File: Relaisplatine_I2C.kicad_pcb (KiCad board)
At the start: 2 copper layers, 85.1 x 107.3 mm, 31 parts, among them J1 J, J1.1 G1-J, J1.2 G1-K, J1001 Conn_01x08, J2 K, J2.1 G2-J, J2.2 G2-K, J3.1 G3-J, J3.2 G3-K, J4.1 G4-J, J4.2 G4-K, J5.1 G5-J, J5.2 G5-K, J6.1 G6-J, J6.2 G6-K, J7.1 G7-J, J7.2 G7-K, J8.1 G8-J, J8.2 G8-K, U1 ULN2803A, U2 PCF8574

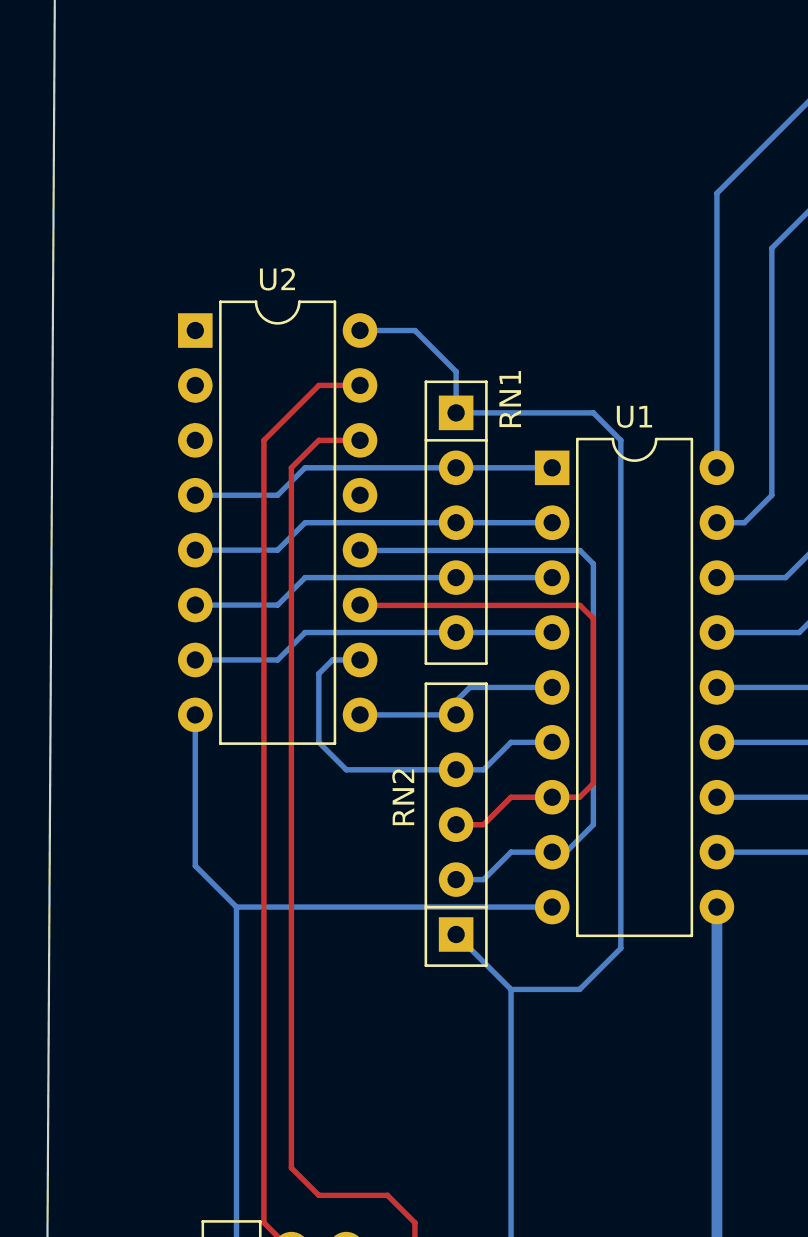
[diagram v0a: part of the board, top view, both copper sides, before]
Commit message: Pins für A0-2 beschltet
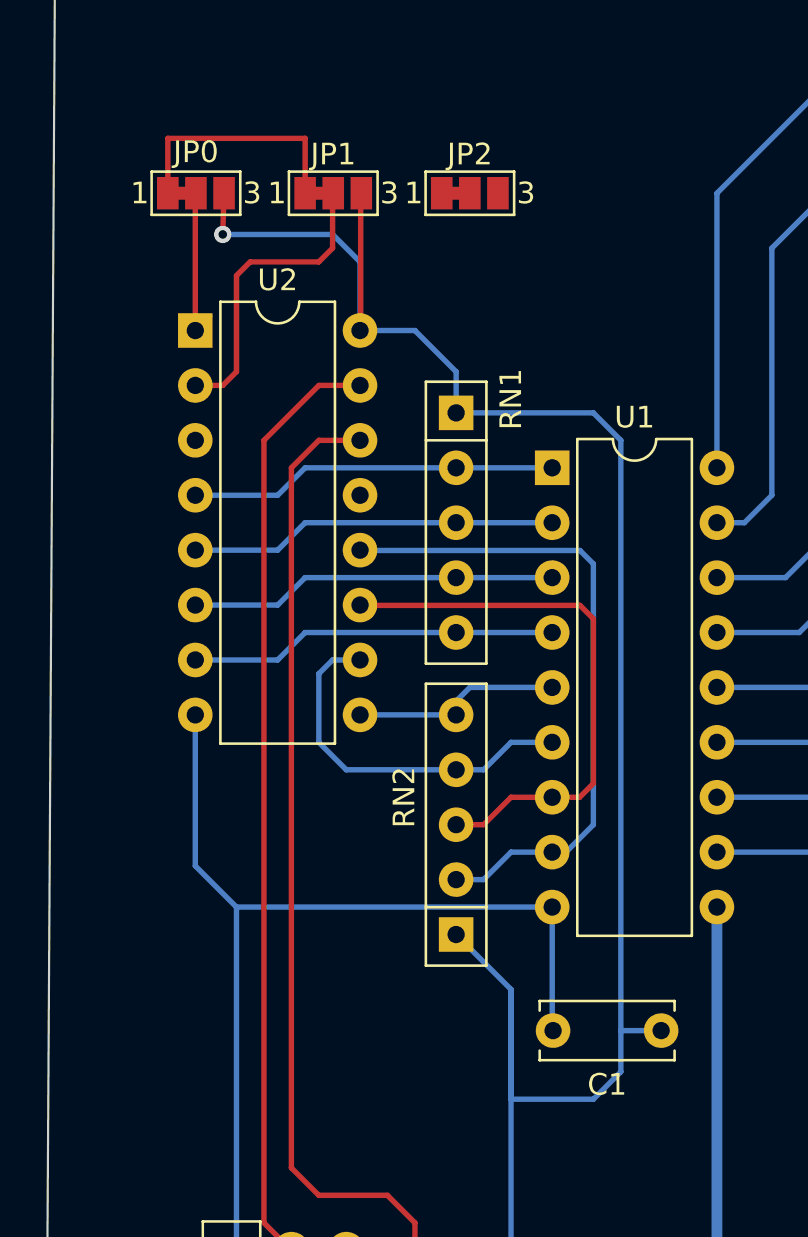
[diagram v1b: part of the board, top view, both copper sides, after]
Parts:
- added C1: 100n, Capacitor_THT:C_Disc_D6.0mm_W2.5mm_P5.00mm, F.Cu at (87.6, 120.0)
- added JP0: SolderJumper_3_Open, Jumper:SolderJumper-3_P1.3mm_Bridged12_Pad1.0x1.5mm_NumberLabels, F.Cu at (66.1, 81.3)
- added JP1: SolderJumper_3_Open, Jumper:SolderJumper-3_P1.3mm_Bridged12_Pad1.0x1.5mm_NumberLabels, F.Cu at (72.4, 81.3)
- added JP2: SolderJumper_3_Open, Jumper:SolderJumper-3_P1.3mm_Bridged12_Pad1.0x1.5mm_NumberLabels, F.Cu at (78.7, 81.3)
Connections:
- U2 pad 1: unconnected-(U2-A0-Pad1) -> Net-(JP0-C)
- U2 pad 2: unconnected-(U2-A1-Pad2) -> Net-(JP1-C)
- U2 pad 3: unconnected-(U2-A2-Pad3) -> Net-(JP2-C)
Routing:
- net +5V: track 72.6 -> 103.4 mm, vias 0 -> 1
- net GND: track 52.5 -> 69.7 mm
- net Net-(JP1-C): track 0.00 -> 14.1 mm
- net Net-(JP0-C): track 0.00 -> 6.63 mm

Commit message: Unbekannte Änderungen
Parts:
- added D1: LED, LED_SMD:LED_0805_2012Metric_Pad1.15x1.40mm_HandSolder, F.Cu at (100.3, 56.9)
- added D2: LED, LED_SMD:LED_0805_2012Metric_Pad1.15x1.40mm_HandSolder, F.Cu at (100.3, 69.6)
- added D3: LED, LED_SMD:LED_0805_2012Metric_Pad1.15x1.40mm_HandSolder, F.Cu at (100.3, 82.3)
- added D4: LED, LED_SMD:LED_0805_2012Metric_Pad1.15x1.40mm_HandSolder, F.Cu at (100.3, 95.0)
- added D5: LED, LED_SMD:LED_0805_2012Metric_Pad1.15x1.40mm_HandSolder, F.Cu at (100.3, 107.7)
- added D6: LED, LED_SMD:LED_0805_2012Metric_Pad1.15x1.40mm_HandSolder, F.Cu at (100.3, 120.4)
- added D7: LED, LED_SMD:LED_0805_2012Metric_Pad1.15x1.40mm_HandSolder, F.Cu at (100.3, 133.1)
- added D8: LED, LED_SMD:LED_0805_2012Metric_Pad1.15x1.40mm_HandSolder, F.Cu at (100.3, 145.8)
- added H1: MountingHole, MountingHole:MountingHole_3.2mm_M3, F.Cu at (67.3, 48.3)
- added H2: MountingHole, MountingHole:MountingHole_3.2mm_M3, F.Cu at (67.3, 154.3)
- added H3: MountingHole, MountingHole:MountingHole_3.2mm_M3, F.Cu at (135.3, 48.3)
- added H4: MountingHole, MountingHole:MountingHole_3.2mm_M3, F.Cu at (135.3, 154.3)
- added J1.1a1001: G1-J, Connector_Pin:Pin_D1.1mm_L8.5mm_W2.5mm_FlatFork, F.Cu at (130.6, 52.7)
- added J1.1a1002: G1-K, Connector_Pin:Pin_D1.1mm_L8.5mm_W2.5mm_FlatFork, F.Cu at (130.6, 86.4)
- added J1.1a1003: G1-K, Connector_Pin:Pin_D1.1mm_L8.5mm_W2.5mm_FlatFork, F.Cu at (130.6, 99.1)
- added J1.1a1004: G1-K, Connector_Pin:Pin_D1.1mm_L8.5mm_W2.5mm_FlatFork, F.Cu at (130.6, 111.8)
- added J1.1a1005: G1-K, Connector_Pin:Pin_D1.1mm_L8.5mm_W2.5mm_FlatFork, F.Cu at (130.6, 124.5)
- added J1.1a1006: G1-K, Connector_Pin:Pin_D1.1mm_L8.5mm_W2.5mm_FlatFork, F.Cu at (130.6, 137.2)
- added J1.1a1007: G1-K, Connector_Pin:Pin_D1.1mm_L8.5mm_W2.5mm_FlatFork, F.Cu at (130.3, 149.9)
- added J1.2a1001: G1-K, Connector_Pin:Pin_D1.1mm_L8.5mm_W2.5mm_FlatFork, F.Cu at (130.6, 61.0)
- added J1.2a1002: G1-J, Connector_Pin:Pin_D1.1mm_L8.5mm_W2.5mm_FlatFork, F.Cu at (130.6, 78.7)
- added J1.2a1003: G1-J, Connector_Pin:Pin_D1.1mm_L8.5mm_W2.5mm_FlatFork, F.Cu at (130.6, 91.4)
- added J1.2a1004: G1-J, Connector_Pin:Pin_D1.1mm_L8.5mm_W2.5mm_FlatFork, F.Cu at (130.6, 104.1)
- added J1.2a1005: G1-J, Connector_Pin:Pin_D1.1mm_L8.5mm_W2.5mm_FlatFork, F.Cu at (130.6, 116.8)
- added J1.2a1006: G1-J, Connector_Pin:Pin_D1.1mm_L8.5mm_W2.5mm_FlatFork, F.Cu at (130.6, 129.5)
- added J1.2a1007: G1-J, Connector_Pin:Pin_D1.1mm_L8.5mm_W2.5mm_FlatFork, F.Cu at (130.6, 142.2)
- added J1001: I²C, Connector_PinHeader_2.54mm:PinHeader_2x02_P2.54mm_Horizontal, F.Cu at (73.0, 147.3)
- added J2.1a1001: G1-J, Connector_Pin:Pin_D1.1mm_L8.5mm_W2.5mm_FlatFork, F.Cu at (130.6, 66.0)
- added J2.2a1001: G2-K, Connector_Pin:Pin_D1.1mm_L8.5mm_W2.5mm_FlatFork, F.Cu at (130.6, 73.7)
- added R1: 1k, Resistor_SMD:R_0805_2012Metric_Pad1.20x1.40mm_HandSolder, F.Cu at (101.3, 61.0)
- added R2: 1k, Resistor_SMD:R_0805_2012Metric_Pad1.20x1.40mm_HandSolder, F.Cu at (101.3, 73.7)
- added R3: 1k, Resistor_SMD:R_0805_2012Metric_Pad1.20x1.40mm_HandSolder, F.Cu at (101.3, 86.4)
- added R4: 1k, Resistor_SMD:R_0805_2012Metric_Pad1.20x1.40mm_HandSolder, F.Cu at (101.4, 99.1)
- added R5: 1k, Resistor_SMD:R_0805_2012Metric_Pad1.20x1.40mm_HandSolder, F.Cu at (101.3, 111.8)
- added R6: 1k, Resistor_SMD:R_0805_2012Metric_Pad1.20x1.40mm_HandSolder, F.Cu at (101.3, 124.5)
- added R7: 1k, Resistor_SMD:R_0805_2012Metric_Pad1.20x1.40mm_HandSolder, F.Cu at (101.3, 137.2)
- added R8: 1k, Resistor_SMD:R_0805_2012Metric_Pad1.20x1.40mm_HandSolder, F.Cu at (101.3, 149.9)
- J1: value J -> K
- J1.1: value G1-J -> G1-K
- J1.2: value G1-K -> G1-J
- J10: renamed from J1001; value Conn_01x08 -> I²C
- J2: value K -> J
- J2.1: value G2-J -> G2-K
- J2.2: value G2-K -> G2-J
- J3.1: value G3-J -> G3-K
- J3.2: value G3-K -> G3-J
- J4.1: value G4-J -> G4-K
- J4.2: value G4-K -> G4-J
- J5.1: value G5-J -> G5-K
- J5.2: value G5-K -> G5-J
- J6.1: value G6-J -> G6-K
- J6.2: value G6-K -> G6-J
- J7.1: value G7-J -> G7-K
- J7.2: value G7-K -> G7-J
- J8.1: value G8-J -> G8-K
- J8.2: value G8-K -> G8-J
- moved C1 50.8 mm to (76.2, 70.5), turned to 0 degrees
- moved A1 41.6 mm to (67.3, 122.6)
- moved A2 37.9 mm to (69.8, 118.1)
- moved A0 36.9 mm to (64.7, 118.1)
- moved U2 25.4 mm to (65.4, 113.0), turned to 90 degrees
- moved RN1 22.2 mm to (69.2, 71.1)
- moved RN2 22.2 mm to (69.2, 95.2)
- moved U1 19.1 mm to (83.8, 74.9)
- moved J1 13.3 mm to (67.3, 63.5)
- moved J2 12.8 mm to (67.3, 55.9)
- moved J8.1 5.21 mm to (138.4, 149.1)
- moved J5.1 5.14 mm to (138.4, 111.3)
- moved J7.1 5.12 mm to (138.4, 136.5)
- moved J6.2 5.12 mm to (138.4, 118.1)
- moved J7.2 5.12 mm to (138.4, 130.8)
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- renumbered JP0 to A0, JP1 to A1, JP2 to A2
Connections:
- RL1 pad 5: unconnected-(RL1-Pad5) -> Net-(J1.2a1001-Pin_1)
- RL1 pad 8: unconnected-(RL1-Pad8) -> Net-(J1.1a1001-Pin_1)
- RL2 pad 5: unconnected-(RL2-Pad5) -> Net-(J2.2a1001-Pin_1)
- RL2 pad 8: unconnected-(RL2-Pad8) -> Net-(J2.1a1001-Pin_1)
- RL3 pad 5: unconnected-(RL3-Pad5) -> Net-(J1.1a1002-Pin_1)
- RL3 pad 8: unconnected-(RL3-Pad8) -> Net-(J1.2a1002-Pin_1)
- RL4 pad 5: unconnected-(RL4-Pad5) -> Net-(J1.1a1003-Pin_1)
- RL4 pad 8: unconnected-(RL4-Pad8) -> Net-(J1.2a1003-Pin_1)
- RL5 pad 5: unconnected-(RL5-Pad5) -> Net-(J1.1a1004-Pin_1)
- RL5 pad 8: unconnected-(RL5-Pad8) -> Net-(J1.2a1004-Pin_1)
- RL6 pad 5: unconnected-(RL6-Pad5) -> Net-(J1.1a1005-Pin_1)
- RL6 pad 8: unconnected-(RL6-Pad8) -> Net-(J1.2a1005-Pin_1)
- RL7 pad 5: unconnected-(RL7-Pad5) -> Net-(J1.1a1006-Pin_1)
- RL7 pad 8: unconnected-(RL7-Pad8) -> Net-(J1.2a1006-Pin_1)
- RL8 pad 5: unconnected-(RL8-Pad5) -> Net-(J1.1a1007-Pin_1)
- RL8 pad 8: unconnected-(RL8-Pad8) -> Net-(J1.2a1007-Pin_1)
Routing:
- net +12V: track 152.1 -> 229.7 mm
- net GND: track 69.7 -> 129.0 mm, vias 0 -> 3
- net Net-(RN1-R1): track 17.0 -> 73.9 mm
- net Net-(RN1-R3): track 17.0 -> 70.5 mm
- net Net-(RN1-R2): track 17.0 -> 62.3 mm
- net Net-(RN1-R4): track 17.0 -> 59.6 mm
- net Net-(RN2-R4): track 9.42 -> 45.5 mm
- net Net-(RN2-R3): track 17.2 -> 40.8 mm
- net +5V: track 103.4 -> 126.9 mm, vias 1 -> 2
- net Net-(D8-K): track 47.6 -> 69.7 mm
- net Net-(D7-K): track 38.3 -> 60.1 mm
- net Net-(D6-K): track 27.2 -> 49.0 mm
- net Net-(D5-K): track 19.8 -> 40.7 mm
- net Net-(J1.1a1004-Pin_1): track 0.00 -> 16.9 mm
- net Net-(J1.1a1002-Pin_1): track 0.00 -> 16.3 mm
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- added copper zone on F.Cu, net +5V
- added copper zone on B.Cu, net GND
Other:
- board size 85.1 x 107.3 mm -> 85.1 x 114.9 mm
- board text added: "+5/12V"
- board text added: "+5V"
- board text added: "G1"
- board text added: "G2"
- board text added: "G3"
- board text added: "G4"
- board text added: "G5"
- board text added: "G6"
- board text added: "G7"
- board text added: "G8"
- board text added: "GND"
- board text added: "Relais"
- board text added: "Relais stromlos"
- board text added: "SCL"
- board text added: "SDA"
- board text added: "©H3-H5N6 2023 I²C Relaisplatine v1.0"

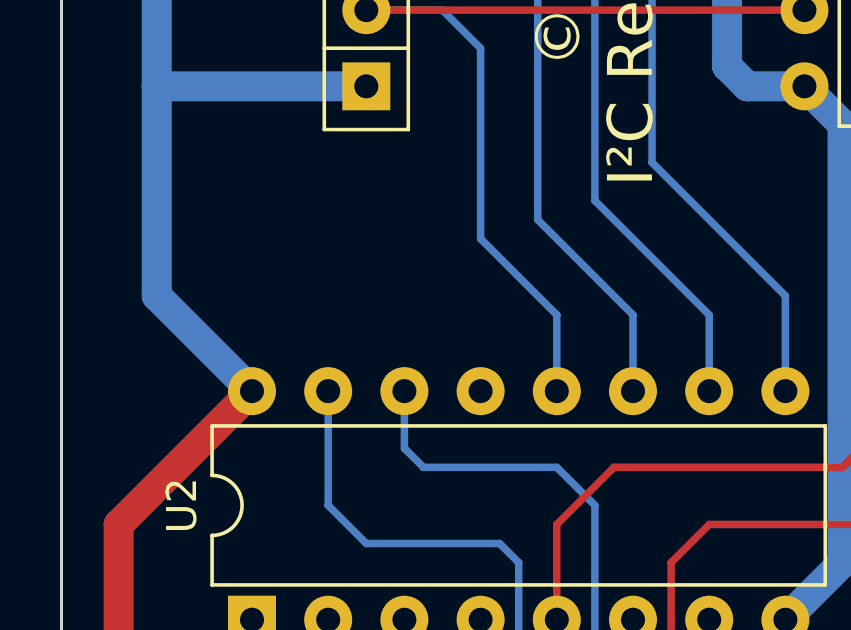
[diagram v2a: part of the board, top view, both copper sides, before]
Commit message: Int-Pin herausgezogen und Kosmetik
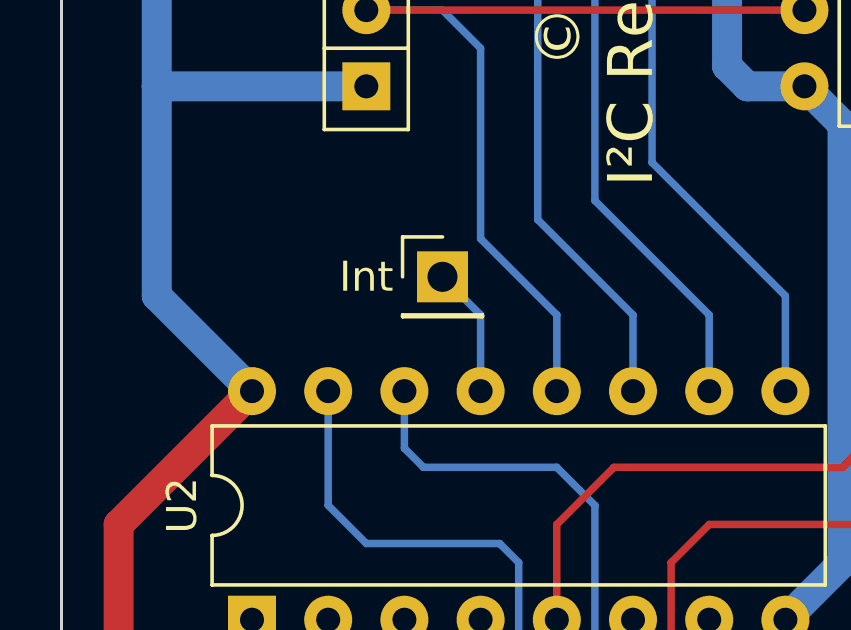
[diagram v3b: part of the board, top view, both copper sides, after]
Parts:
- added J12: Int, Connector_PinHeader_2.54mm:PinHeader_1x01_P2.54mm_Vertical, F.Cu at (71.8, 101.6)
- added Tx1: ©H3-H5N6 2023 I²C Relaisplatine v1.0, Text:Text, F.Cu at (103.8, 46.0)
- J11: renamed from J1001; value I²C -> Relais-Power
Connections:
- U2 pad 13: unconnected-(U2-~{INT}-Pad13) -> Net-(J12-Pin_1)
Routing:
- net Net-(J12-Pin_1): track 0.00 -> 4.34 mm
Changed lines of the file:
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@@
   (net 16 "Net-(A2-C)")
   (net 17 "Net-(A1-C)")
-  (net 18 "unconnected-(U2-~{INT}-Pad13)")
+  (net 18 "Net-(J12-Pin_1)")
   (net 19 "Net-(J1-Pin_1)")
   (net 20 "Net-(J5.2-Pin_1)")
@@
       (net 11 "Net-(J2.2-Pin_1)") (pinfunction "Pin_1") (pintype "passive"))
   )
+  (footprint "Text:Text" (layer "F.Cu")
+    (at 103.759 45.974)
+    (descr "Text F+B")
+    (tags "text")
+    (property "Sheetfile" "Relaisplatine_I2C.kicad_sch")
+    (property "Sheetname" "")
+    (property "ki_description" "Mounting Hole without connection")
+    (property "ki_keywords" "mounting hole")
+    (attr exclude_from_pos_files)
+    (fp_text reference "Tx1" (at 0 -2.286) (layer "F.Fab")
+        (effects (font (size 1 1) (thickness 0.15)))
+    )
+    (fp_text value "©H3-H5N6 2023 I²C Relaisplatine v1.0" (at 0 3.2) (layer "F.Fab")
+        (effects (font (size 1 1) (thickness 0.15)))
+    )
+    (fp_text user "${VALUE}" (at 0.127 0) (layer "B.SilkS")
+        (effects (font (size 1.5 1.5) (thickness 0.3) bold) (justify mirror))
+    )
+    (fp_text user "${VALUE}" (at 0 0) (layer "F.SilkS")
+        (effects (font (size 1.5 1.5) (thickness 0.3) bold))
+    )
+  )
   (footprint "Resistor_SMD:R_0805_2012Metric_Pad1.20x1.40mm_HandSolder" (layer "F.Cu")
     (at 101.346 124.46 180)
@@
     )
   )
+  (footprint "Connector_PinHeader_2.54mm:PinHeader_1x01_P2.54mm_Vertical" (layer "F.Cu")
+    (at 71.755 101.6)
+    (descr "Through hole straight pin header, 1x01, 2.54mm pitch, single row")
+    (tags "Through hole pin header THT 1x01 2.54mm single row")
+    (property "Sheetfile" "Relaisplatine_I2C.kicad_sch")
+    (property "Sheetname" "")
+    (property "ki_description" "Generic connector, single row, 01x01, script generated")
+    (property "ki_keywords" "connector")
+    (attr through_hole)
+    (fp_text reference "J12" (at 0 -2.33) (layer "F.SilkS") hide
+        (effects (font (size 1 1) (thickness 0.15)))
+    )
+    (fp_text value "Int" (at -2.54 0) (layer "F.SilkS")
+        (effects (font (size 1 1) (thickness 0.15)))
+    )
+    (fp_text user "${REFERENCE}" (at 0 0 90) (layer "F.Fab")
+        (effects (font (size 1 1) (thickness 0.15)))
+    )
+    (fp_line (start -1.33 -1.33) (end 0 -1.33)
+      (stroke (width 0.12) (type solid)) (layer "F.SilkS"))
+    (fp_line (start -1.33 0) (end -1.33 -1.33)
+      (stroke (width 0.12) (type solid)) (layer "F.SilkS"))
+    (fp_line (start -1.33 1.27) (end -1.33 1.33)
+      (stroke (width 0.12) (type solid)) (layer "F.SilkS"))
+    (fp_line (start -1.33 1.27) (end 1.33 1.27)
+      (stroke (width 0.12) (type solid)) (layer "F.SilkS"))
+    (fp_line (start -1.33 1.33) (end 1.33 1.33)
+      (stroke (width 0.12) (type solid)) (layer "F.SilkS"))
+    (fp_line (start 1.33 1.27) (end 1.33 1.33)
+      (stroke (width 0.12) (type solid)) (layer "F.SilkS"))
+    (fp_line (start -1.8 -1.8) (end -1.8 1.8)
+      (stroke (width 0.05) (type solid)) (layer "F.CrtYd"))
+    (fp_line (start -1.8 1.8) (end 1.8 1.8)
+      (stroke (width 0.05) (type solid)) (layer "F.CrtYd"))
+    (fp_line (start 1.8 -1.8) (end -1.8 -1.8)
+      (stroke (width 0.05) (type solid)) (layer "F.CrtYd"))
+    (fp_line (start 1.8 1.8) (end 1.8 -1.8)
+      (stroke (width 0.05) (type solid)) (layer "F.CrtYd"))
+    (fp_line (start -1.27 -0.635) (end -0.635 -1.27)
+      (stroke (width 0.1) (type solid)) (layer "F.Fab"))
+    (fp_line (start -1.27 1.27) (end -1.27 -0.635)
+      (stroke (width 0.1) (type solid)) (layer "F.Fab"))
+    (fp_line (start -0.635 -1.27) (end 1.27 -1.27)
+      (stroke (width 0.1) (type solid)) (layer "F.Fab"))
+    (fp_line (start 1.27 -1.27) (end 1.27 1.27)
+      (stroke (width 0.1) (type solid)) (layer "F.Fab"))
+    (fp_line (start 1.27 1.27) (end -1.27 1.27)
+      (stroke (width 0.1) (type solid)) (layer "F.Fab"))
+    (pad "1" thru_hole rect (at 0 0) (size 1.7 1.7) (drill 1) (layers "*.Cu" "*.Mask")
+      (net 18 "Net-(J12-Pin_1)") (pinfunction "Pin_1") (pintype "passive"))
+    (model "${KICAD6_3DMODEL_DIR}/Connector_PinHeader_2.54mm.3dshapes/PinHeader_1x01_P2.54mm_Vertical.wrl"
+      (offset (xyz 0 0 0))
+      (scale (xyz 1 1 1))
+      (rotate (xyz 0 0 0))
+    )
+  )
   (footprint "Package_DIP:DIP-18_W7.62mm" (layer "F.Cu")
     (at 83.82 74.93)
@@
     (property "ki_keywords" "connector")
     (attr through_hole)
-    (fp_text reference "J1001" (at 5.655 -2.27) (layer "F.SilkS") hide
+    (fp_text reference "J11" (at 5.655 -2.27) (layer "F.SilkS") hide
         (effects (font (size 1 1) (thickness 0.15)))
     )
-    (fp_text value "I²C" (at 5.655 4.81) (layer "F.Fab")
+    (fp_text value "Relais-Power" (at 5.655 4.81) (layer "F.Fab")
         (effects (font (size 1 1) (thickness 0.15)))
     )
@@
       (net 36 "Net-(RN2-R1)") (pinfunction "P7") (pintype "bidirectional"))
     (pad "13" thru_hole oval (at 7.62 7.62 90) (size 1.6 1.6) (drill 0.8) (layers "*.Cu" "*.Mask")
-      (net 18 "unconnected-(U2-~{INT}-Pad13)") (pinfunction "~{INT}") (pintype "open_collector+no_connect"))
+      (net 18 "Net-(J12-Pin_1)") (pinfunction "~{INT}") (pintype "open_collector"))
     (pad "14" thru_hole oval (at 7.62 5.08 90) (size 1.6 1.6) (drill 0.8) (layers "*.Cu" "*.Mask")
       (net 40 "Net-(J10-Pin_5)") (pinfunction "SCL") (pintype "input"))
@@
   (gr_line (start 144.145 158.75) (end 59.055 158.75)
     (stroke (width 0.1) (type default)) (layer "Edge.Cuts"))
-  (gr_text "©H3-H5N6 2023 I²C Relaisplatine v1.0\n" (at 100.33 46.228) (layer "B.SilkS")
-    (effects (font (size 1.5 1.5) (thickness 0.3)) (justify mirror))
-  )
   (gr_text "G7" (at 94.012 133.858) (layer "F.SilkS")
     (effects (font (size 1.5 1.5) (thickness 0.3) bold) (justify left bottom))
@@
   (segment (start 67.31 115.57) (end 67.31 122.525) (width 0.25) (layer "F.Cu") (net 17))
   (segment (start 67.945 114.935) (end 67.31 115.57) (width 0.25) (layer "F.Cu") (net 17))
+  (segment (start 71.755 101.6) (end 73.025 102.87) (width 0.25) (layer "B.Cu") (net 18))
+  (segment (start 73.025 102.87) (end 73.025 105.41) (width 0.25) (layer "B.Cu") (net 18))
   (segment (start 97.155 127) (end 113.665 127) (width 1) (layer "F.Cu") (net 19))
   (segment (start 97.155 114.3) (end 113.665 114.3) (width 1) (layer "F.Cu") (net 19))
